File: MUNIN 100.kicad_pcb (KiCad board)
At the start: 2 copper layers, 100 x 80 mm, 83 parts, among them IC1 ACHS-7123, J1 TX_IN, J2 Conn_Coaxial, J3 Conn_01x03_Male, J4 Conn_01x01_Pin, J5 Conn_01x01_Pin, Q1 ISS55EP06LMXTSA1, Q2 MRF101AN, Q3 MRF101BN, U2 LM358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

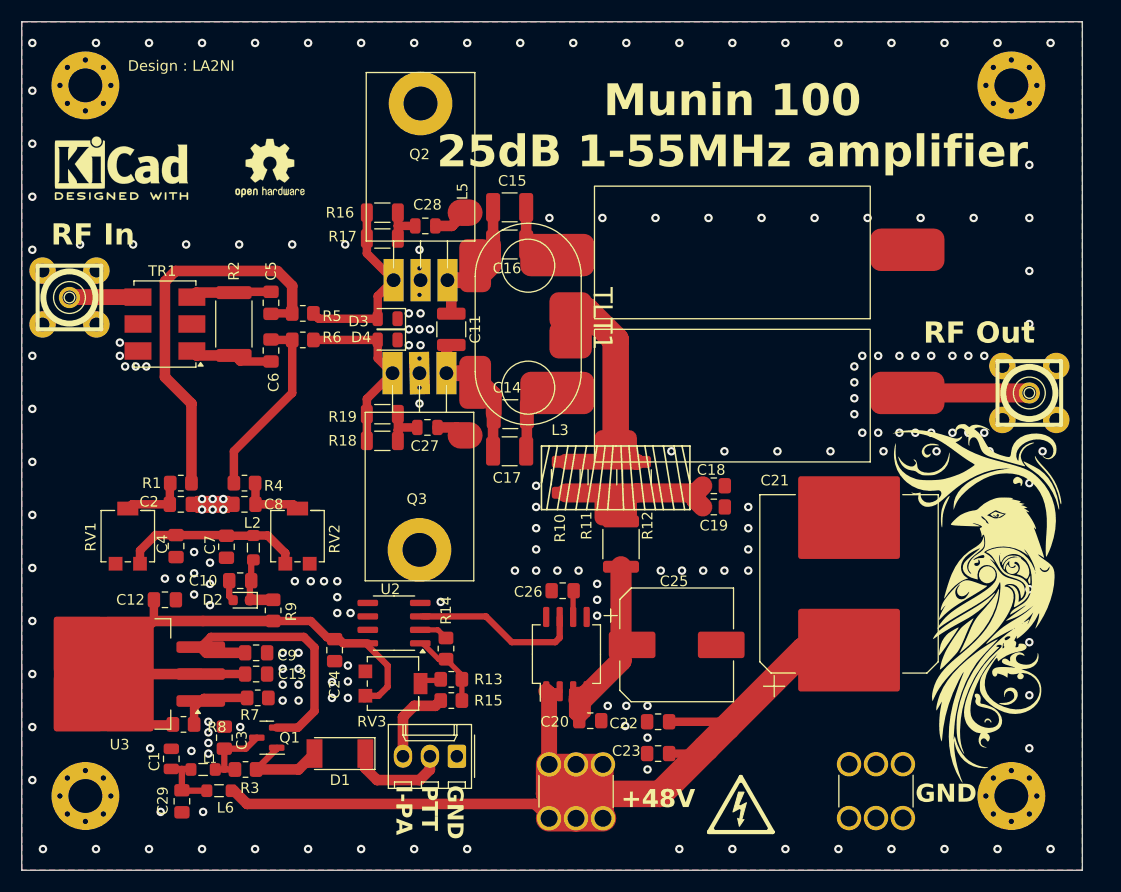
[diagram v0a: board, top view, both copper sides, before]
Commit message: minor errors fixed, Gerber is out of date
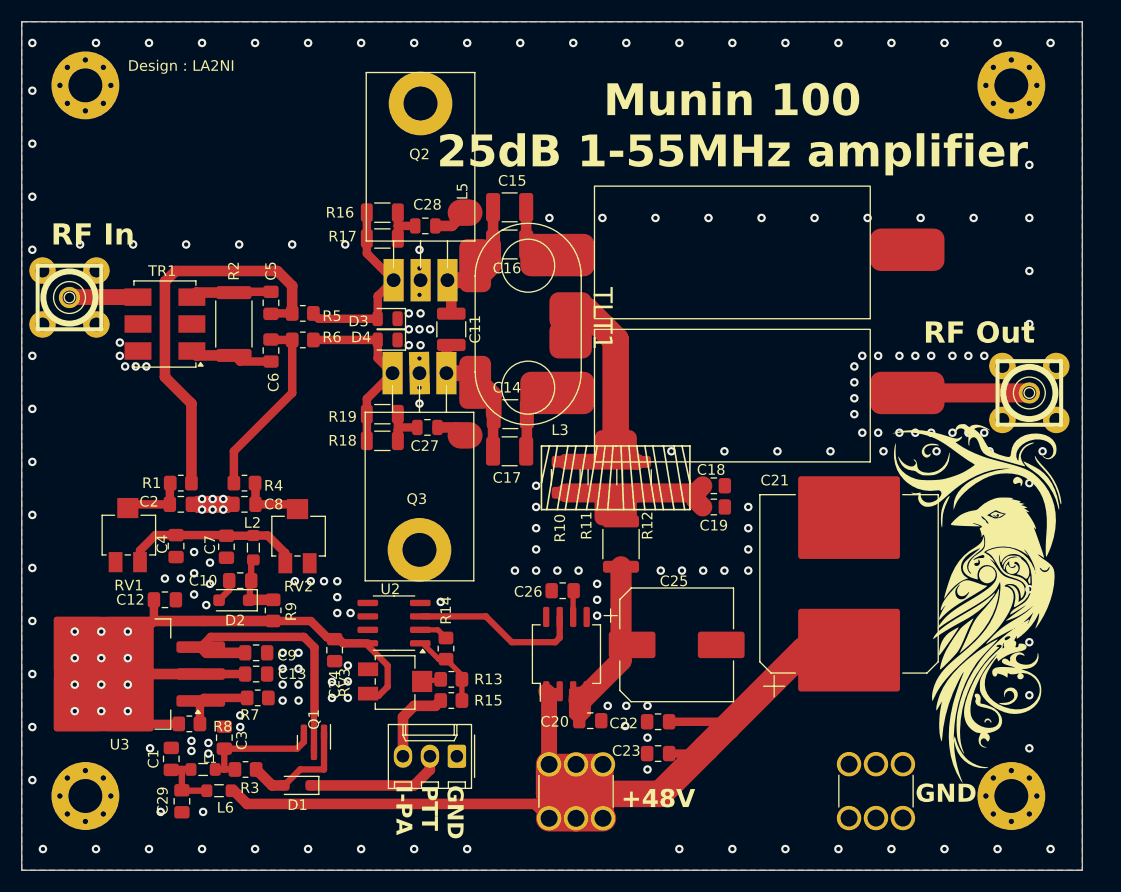
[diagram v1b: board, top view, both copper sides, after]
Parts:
- removed REF**: OSHW-Logo2_7.3x6mm_SilkScreen, Symbol:OSHW-Logo2_7.3x6mm_SilkScreen
- removed REF**: Symbol_HighVoltage_Triangle_6x6mm_Copper, logo:Symbol_HighVoltage_Triangle_6x6mm_Copper
- removed REF**: KiCad-Logo2_5mm_SilkScreen, Symbol:KiCad-Logo2_5mm_SilkScreen
- C1: value 100n -> 100n hv; footprint Capacitor_SMD:C_0805_2012Metric -> Capacitor_SMD:C_0805_2012Metric_Pad1.18x1.45mm_HandSolder
- C14, C15, C16, C17: value 100n -> 100n hf
- C18, C19, C20, C23, C29, C3, C9: value 100n -> 100n hv
- C27, C28: value 100nH -> 100n
- D1: value BAT54J -> SS36; footprint Diode_SMD:D_MELF -> Diode_SMD:D_SOD-323_HandSoldering
- D2: footprint Diode_SMD:D_0603_1608Metric -> Diode_SMD:D_SOD-123F
- J3: value Conn_01x03_Male -> Molex kk 2.54-3
- R1, R4: value 100R -> 100R (or 22R)
- R16, R17, R18, R19: value TBD -> 1k2
- RV1, RV2, RV3: footprint Potentiometer_SMD:Potentiometer_Bourns_3214G_Horizontal -> Potentiometer_SMD:Potentiometer_Bourns_3214X_Vertical
- moved D1 5.00 mm to (71.0, 147.0)
- moved Q1 4.47 mm to (72.5, 142.9), turned to -90 degrees
- moved D2 0.72 mm to (65.0, 129.5)
- moved R8 0.55 mm to (60.8, 141.2)
- moved RV3 0.28 mm to (80.2, 137.2), turned to 90 degrees
- moved RV1 0.10 mm to (55.0, 123.4), turned to 180 degrees
- turned RV2 to 180 degrees
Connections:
- C3 pad 1: Net-(Q1-D) -> Net-(Q1-S)
- C9 pad 1: Net-(Q1-S) -> Net-(Q1-D)
- L1 pad 2: Net-(Q1-D) -> Net-(Q1-S)
- Q2 pad : GND -> (no net)
- Q3 pad : GND -> (no net)
- R3 pad 1: Net-(Q1-D) -> Net-(Q1-S)
- RV1 pad 1: Net-(C4-Pad1) -> GND
- RV1 pad 3: GND -> Net-(C4-Pad1)
- RV2 pad 1: GND -> Net-(C4-Pad1)
- RV2 pad 3: Net-(C4-Pad1) -> GND
- RV3 pad 1: +5V -> GND
- RV3 pad 3: GND -> +5V
- U3 pad 3: Net-(Q1-S) -> Net-(Q1-D)
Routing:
- net Net-(Q1-D): track 7.30 -> 25.8 mm
- net Net-(Q1-S): track 26.2 -> 12.5 mm
- net Net-(D1-K): track 9.61 -> 13.1 mm
- net Net-(D1-A): track 8.97 -> 11.1 mm
- net +5V: track 55.3 -> 56.6 mm, vias 0 -> 12

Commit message: new 48V trace
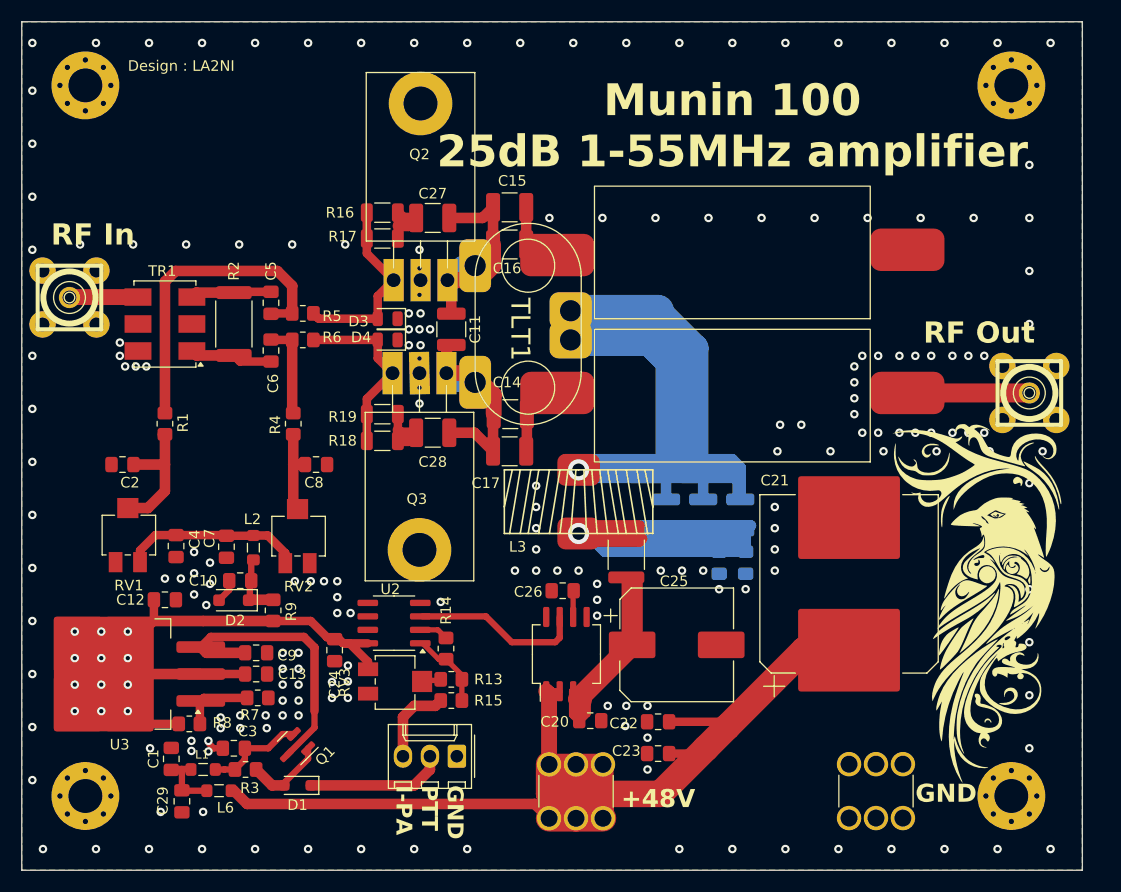
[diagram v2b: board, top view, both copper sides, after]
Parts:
- removed L5: 1 T, Resistor_THT:R_Axial_DIN0918_L18.0mm_D9.0mm_P30.48mm_Horizontal
- C18, C19, R10, R11, R12: moved to B.Cu
- C27, C28: value 100n -> 100n hf; footprint Capacitor_SMD:C_0805_2012Metric -> Capacitor_SMD:C_1210_3225Metric_Pad1.33x2.70mm_HandSolder
- moved C27 19.8 mm to (83.8, 93.5)
- moved C28 19.5 mm to (83.8, 113.8)
- moved R11 13.5 mm to (112.8, 121.5)
- moved R10 13.4 mm to (109.2, 121.5)
- moved C18 7.85 mm to (113.2, 126.0), turned to 90 degrees
- moved C8 7.72 mm to (72.8, 116.8), turned to 180 degrees
- moved R4 7.25 mm to (70.6, 112.9), turned to -90 degrees
- moved C2 6.66 mm to (54.5, 116.8), turned to 0 degrees
- moved R1 5.80 mm to (58.5, 112.9), turned to -90 degrees
- moved C19 5.27 mm to (110.8, 126.0), turned to 90 degrees
- moved R12 4.48 mm to (105.8, 121.5)
- moved L3 4.16 mm to (97.5, 120.2)
- moved Q1 1.96 mm to (70.7, 143.5), turned to -135 degrees
- moved C3 1.35 mm to (65.0, 143.5), turned to 180 degrees
- moved L4 1.12 mm to (102.0, 125.2)
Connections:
- C27 pad 2: Net-(C27-Pad2) -> Net-(Q2-D)
- C28 pad 2: Net-(C28-Pad2) -> Net-(Q3-D)
- Q2 pad : (no net) -> GND
- Q3 pad : (no net) -> GND
- R16 pad 2: Net-(C28-Pad1) -> Net-(C27-Pad1)
- R17 pad 2: Net-(C28-Pad1) -> Net-(C27-Pad1)
- R18 pad 2: Net-(C27-Pad1) -> Net-(C28-Pad1)
- R19 pad 2: Net-(C27-Pad1) -> Net-(C28-Pad1)
- RV3 pad 1: GND -> +5V
- RV3 pad 3: +5V -> GND
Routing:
- net Net-(L3-Pad1): track 22.1 -> 113.8 mm, vias 0 -> 1
- net Net-(C18-Pad2): track 14.8 -> 91.6 mm, vias 0 -> 1
- net GND: track 23.9 -> 4.18 mm, vias 190 -> 191
- net Net-(C6-Pad2): track 17.8 -> 8.96 mm
- net Net-(Q3-D): track 13.5 -> 21.4 mm
- net Net-(Q2-D): track 13.2 -> 20.9 mm
- net Net-(C5-Pad2): track 37.6 -> 30.0 mm
- net Net-(C2-Pad2): track 6.14 -> 13.2 mm
- net +5V: track 56.6 -> 52.9 mm
- net Net-(D1-A): track 11.1 -> 7.70 mm
- net Net-(C28-Pad2): track 3.32 -> 0.00 mm
- net Net-(C27-Pad2): track 2.91 -> 0.00 mm
- net Net-(C8-Pad2): track 6.14 -> 8.89 mm
- net Net-(Q1-S): track 12.5 -> 9.83 mm
- net Net-(C28-Pad1): track 4.08 -> 6.38 mm
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
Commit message: 48V rail, kicad 8.03, no new gerber
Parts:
- moved J2 2.76 mm to (140.2, 107.2)
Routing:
- net +5V: track 52.9 -> 71.4 mm, vias 12 -> 20
- net Net-(J2-In): track 11.5 -> 7.50 mm
- net GND: vias 191 -> 197

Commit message: third release, new power TLT
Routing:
- net Net-(J4-Pin_1): track 120.6 -> 182.6 mm
- net Net-(L3-Pad1): track 113.8 -> 126.2 mm

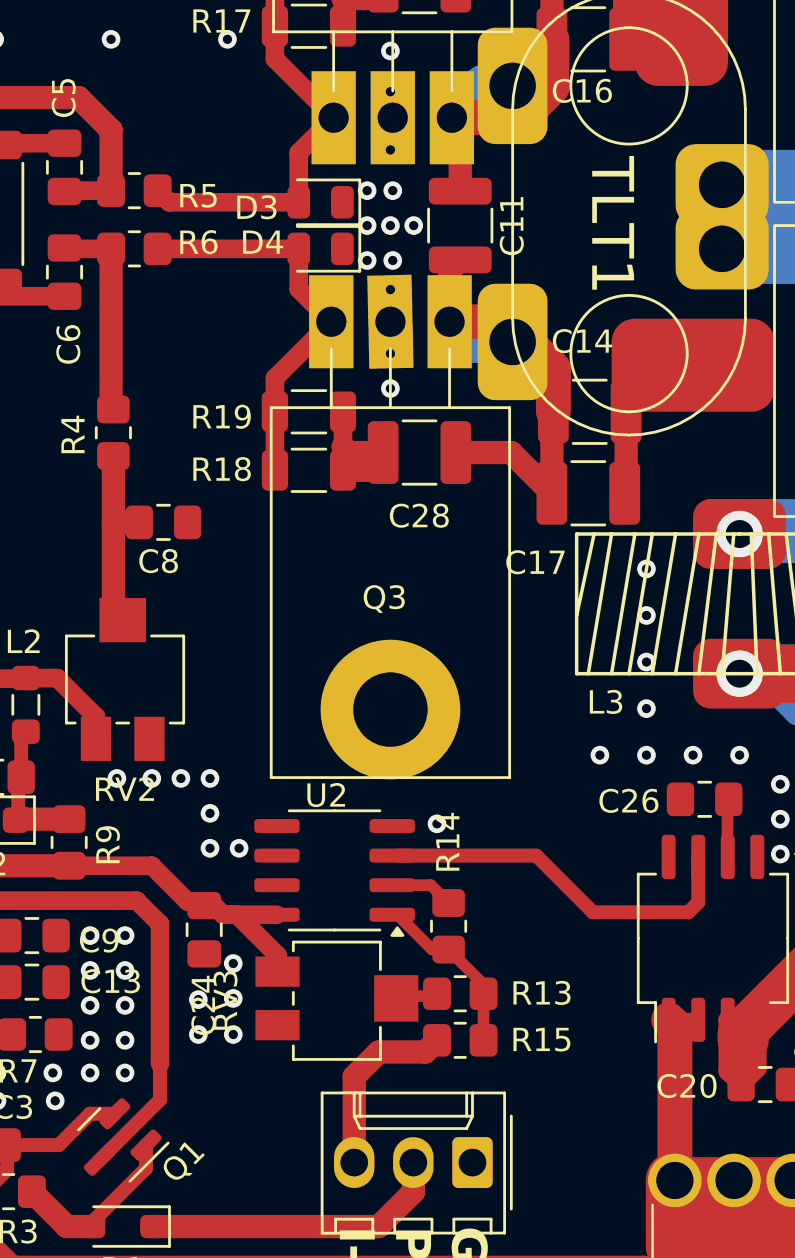
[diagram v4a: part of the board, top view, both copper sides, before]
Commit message: kicad10 update, minor schematic changes
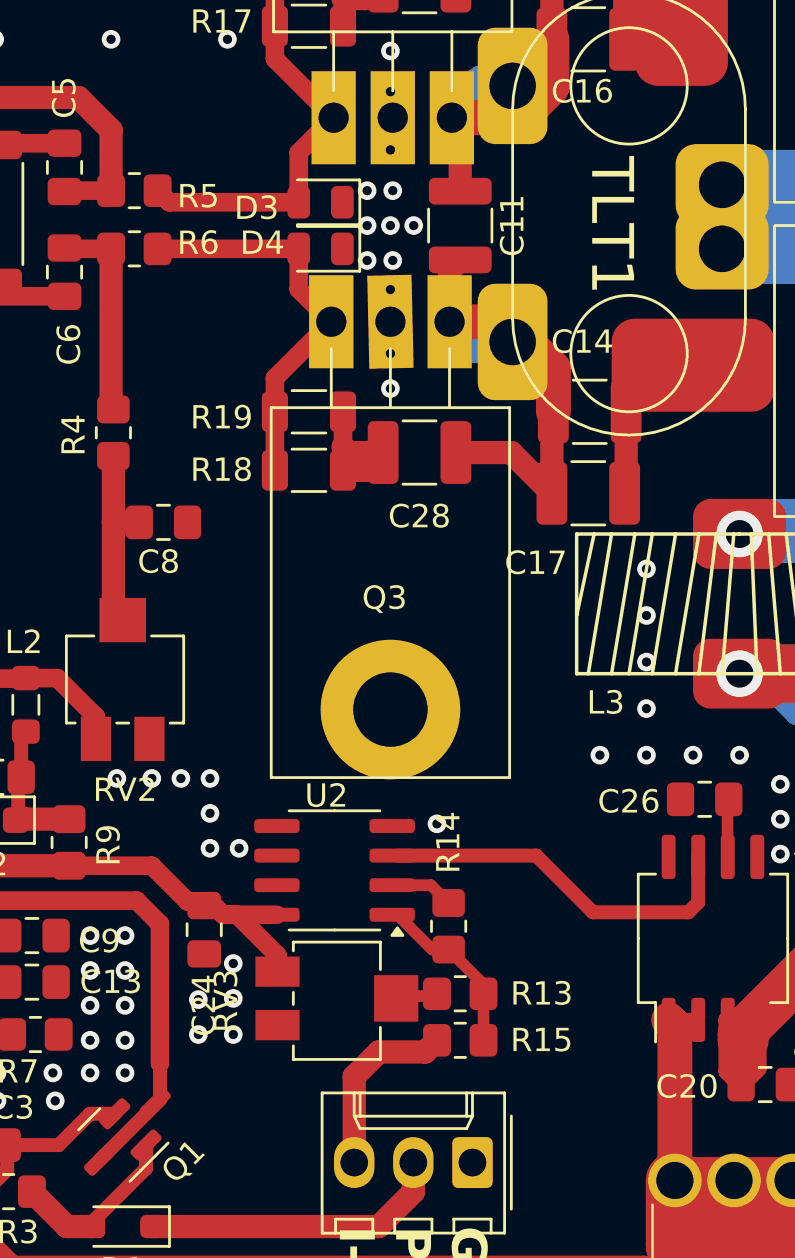
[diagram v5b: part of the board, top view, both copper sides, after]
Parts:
- added ?: , , F.Cu at (72.4, 141.7)
